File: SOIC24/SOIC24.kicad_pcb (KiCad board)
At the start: 2 copper layers, 30.5 x 17.8 mm, 9 parts, among them J1 Conn_01x12, J2 Conn_02x12_Counter_Clockwise, J3 Conn_02x12_Counter_Clockwise, J4 Conn_02x12_Counter_Clockwise, J5 Conn_01x12, J6 Conn_01x05

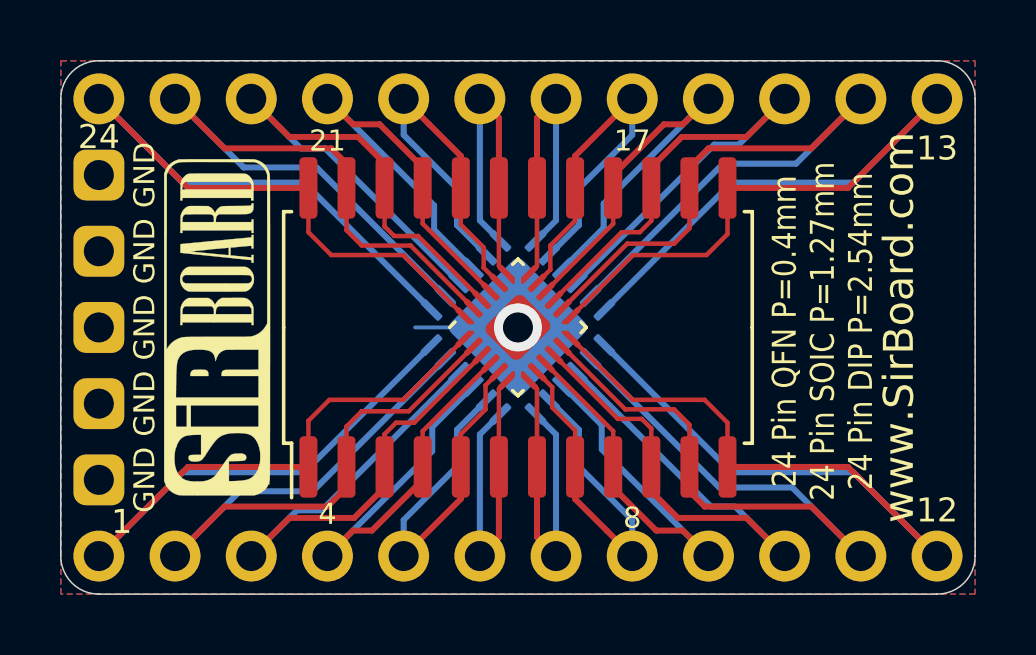
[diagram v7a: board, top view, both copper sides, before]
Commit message: Breakout Boards Revision 2
Renders updated, silkscreen text improved, blurry silkscreen items removed/resized.
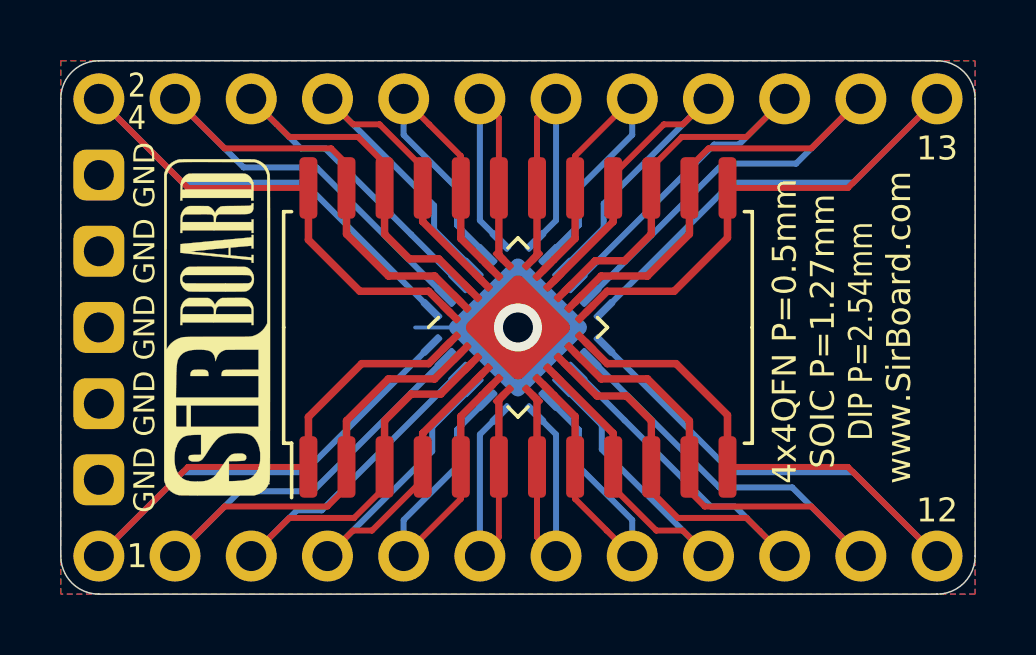
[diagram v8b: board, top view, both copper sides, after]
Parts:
- added REF**: OSHW-Logo2_7.3x6mm_SilkScreen, Symbol:OSHW-Logo2_7.3x6mm_SilkScreen, B.Cu at (62.4, 40.9)
- J2: footprint Package_DFN_QFN:QFN-24-1EP_3x3mm_P0.4mm_EP1.75x1.6mm -> Package_DFN_QFN:QFN-24-1EP_4x4mm_P0.5mm_EP2.6x2.6mm
- moved G*** 15.5 mm to (79.0, 34.3), turned to 0 degrees
- moved G*** 2.95 mm to (79.2, 40.4), turned to 0 degrees
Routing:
- net Net-(J1-Pad9): track 16.9 -> 12.5 mm
- net Net-(J1-Pad8): track 13.8 -> 10.1 mm
- net Net-(J2-Pad21): track 16.9 -> 20.3 mm
- net Net-(J2-Pad20): track 13.8 -> 16.5 mm
- net Net-(J2-Pad19): track 11.3 -> 10.7 mm
- net Net-(J2-Pad18): track 11.3 -> 10.7 mm
- net Net-(J1-Pad7): track 11.3 -> 10.7 mm
- net Net-(J1-Pad6): track 11.3 -> 10.7 mm
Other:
- board text added: "2"
- board text added: "20"
- board text added: "4x4QFN P=0.5mm"
- board text added: "5"
- board text added: "5x5QFN P=0.65mm"
- board text added: "DIP P=2.54mm"
- board text added: "SOIC P=1.27mm"
- board text removed: "21"
- board text removed: "24"
- board text removed: "24 Pin 5x5 QFN P=0.65mm"
- board text removed: "24 Pin DIP P=2.54mm"
- board text removed: "24 Pin QFN P=0.4mm"
- board text removed: "24 Pin SOIC P=1.27mm"
